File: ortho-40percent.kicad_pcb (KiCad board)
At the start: 2 copper layers, 229 x 81 mm, 128 parts, among them J1 USB-C_Receptacle-24, SW1 SW_NO_4-Pin, SW10 CherryMX, SW11 CherryMX, SW12 CherryMX, SW13 CherryMX, SW14 CherryMX, SW15 CherryMX, SW16 CherryMX, SW17 CherryMX, SW18 CherryMX, SW19 CherryMX, SW2 CherryMX, SW20 CherryMX, SW21 CherryMX, SW22 CherryMX, SW23 CherryMX, SW24 CherryMX, SW25 CherryMX, SW26 CherryMX, SW27 CherryMX, SW28 CherryMX, SW29 CherryMX, SW3 CherryMX, SW30 CherryMX, SW31 CherryMX, SW32 CherryMX, SW33 CherryMX, SW34 CherryMX, SW35 CherryMX, SW36 CherryMX, SW37 CherryMX, SW38 CherryMX, SW39 CherryMX, SW4 CherryMX, SW40 CherryMX, SW41 CherryMX, SW42 CherryMX, SW43 CherryMX, SW44 CherryMX, SW45 CherryMX, SW46 CherryMX, SW47 CherryMX, SW48 CherryMX, SW49 CherryMX, SW5 CherryMX, SW50 CherryMX, SW51 CherryMX, SW6 CherryMX, SW7 CherryMX, SW8 CherryMX, SW9 CherryMX, U1 U_TPD4E05U06DQAR, U2 U_ATmega32u4-MU, Y1 XTAL_4Lead

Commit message: Routing
more routing and placement
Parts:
- moved C4 57.4 mm to (210.0, 186.9)
- moved C5 56.2 mm to (213.0, 182.9)
- moved C1 54.5 mm to (215.0, 186.4), turned to 180 degrees
- moved C8 53.1 mm to (225.0, 187.4), turned to 90 degrees
- moved C7 49.7 mm to (237.0, 187.4), turned to 90 degrees
- moved Y1 47.8 mm to (219.0, 184.9)
- moved C2 47.5 mm to (215.0, 183.9), turned to 180 degrees
- moved C9 45.4 mm to (237.0, 181.9)
- moved C6 41.0 mm to (225.0, 182.4), turned to 270 degrees
- moved D34 10.7 mm to (204.5, 184.9)
- moved U2 8.51 mm to (231.0, 185.4), turned to 270 degrees
- moved R4 6.58 mm to (230.0, 178.9)
- moved R3 6.52 mm to (232.0, 178.9)
- moved D35 4.72 mm to (247.0, 190.9)
- moved L1 1.50 mm to (238.0, 167.4), turned to 90 degrees
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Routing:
- net VCC: track 0.00 -> 30.0 mm, vias 0 -> 6
- net DA+: track 0.00 -> 16.3 mm, vias 0 -> 2
- net DA-: track 0.00 -> 15.9 mm, vias 0 -> 2
- net VBUS: track 0.00 -> 7.28 mm, vias 0 -> 1
- net /D-: track 3.22 -> 6.30 mm
- net GND: track 1.42 -> 4.34 mm, vias 1 -> 0
- net /D+: track 6.30 -> 4.26 mm
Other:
- net class USB_diffPair added: clearance 0.2, trace_width 0.25, via_dia 0.8, via_drill 0.4

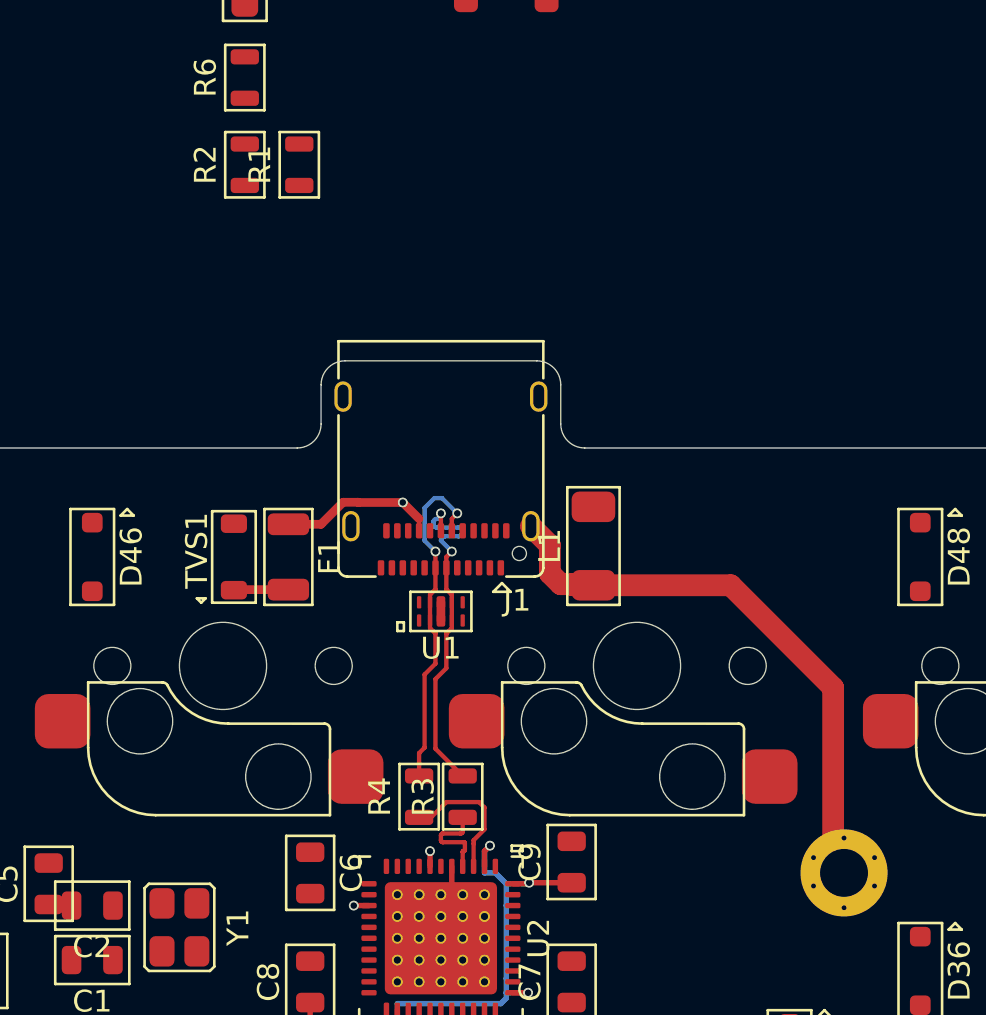
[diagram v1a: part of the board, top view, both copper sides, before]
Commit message: USB connections
Completed USB-C routing, tested ground planes and settings for robustness
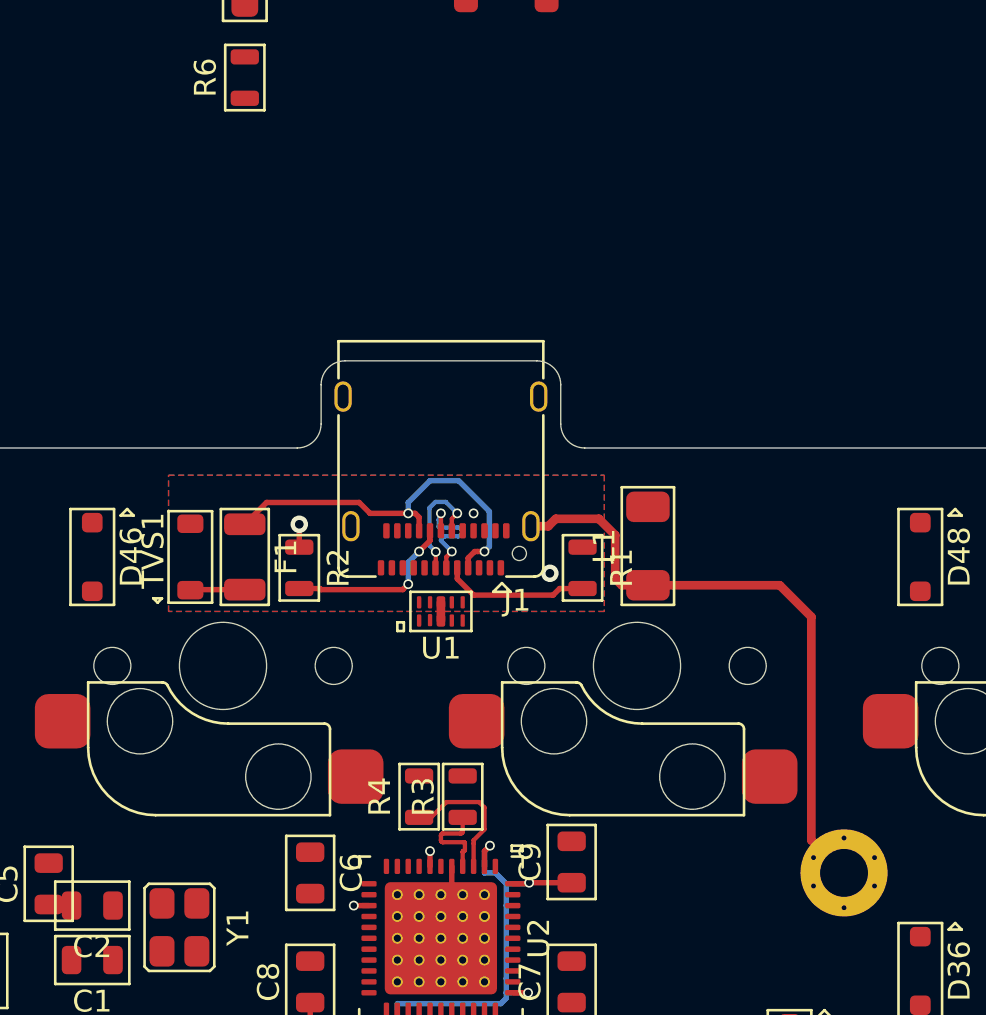
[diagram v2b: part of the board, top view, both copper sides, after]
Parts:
- moved R1 22.6 mm to (237.5, 168.4), turned to 270 degrees
- moved R2 18.7 mm to (224.5, 168.4), turned to 270 degrees
- moved L1 2.50 mm to (240.5, 167.4)
- moved F1 2.00 mm to (222.0, 167.9)
- moved TVS1 2.00 mm to (219.5, 167.9)
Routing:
- net DA+: track 16.3 -> 5.44 mm
- net DA-: track 15.9 -> 5.39 mm
- net VBUS: track 7.28 -> 17.8 mm, vias 1 -> 2
- net Net-(J1-PadB5): track 0.00 -> 7.99 mm, vias 0 -> 2
- net Net-(J1-PadA5): track 0.00 -> 6.68 mm
- net GNDPWR: track 26.4 -> 28.4 mm
- net GND: track 4.34 -> 5.39 mm, vias 0 -> 3
- added copper zone on B.Cu, net GND
- added copper zone on F.Cu, net GND

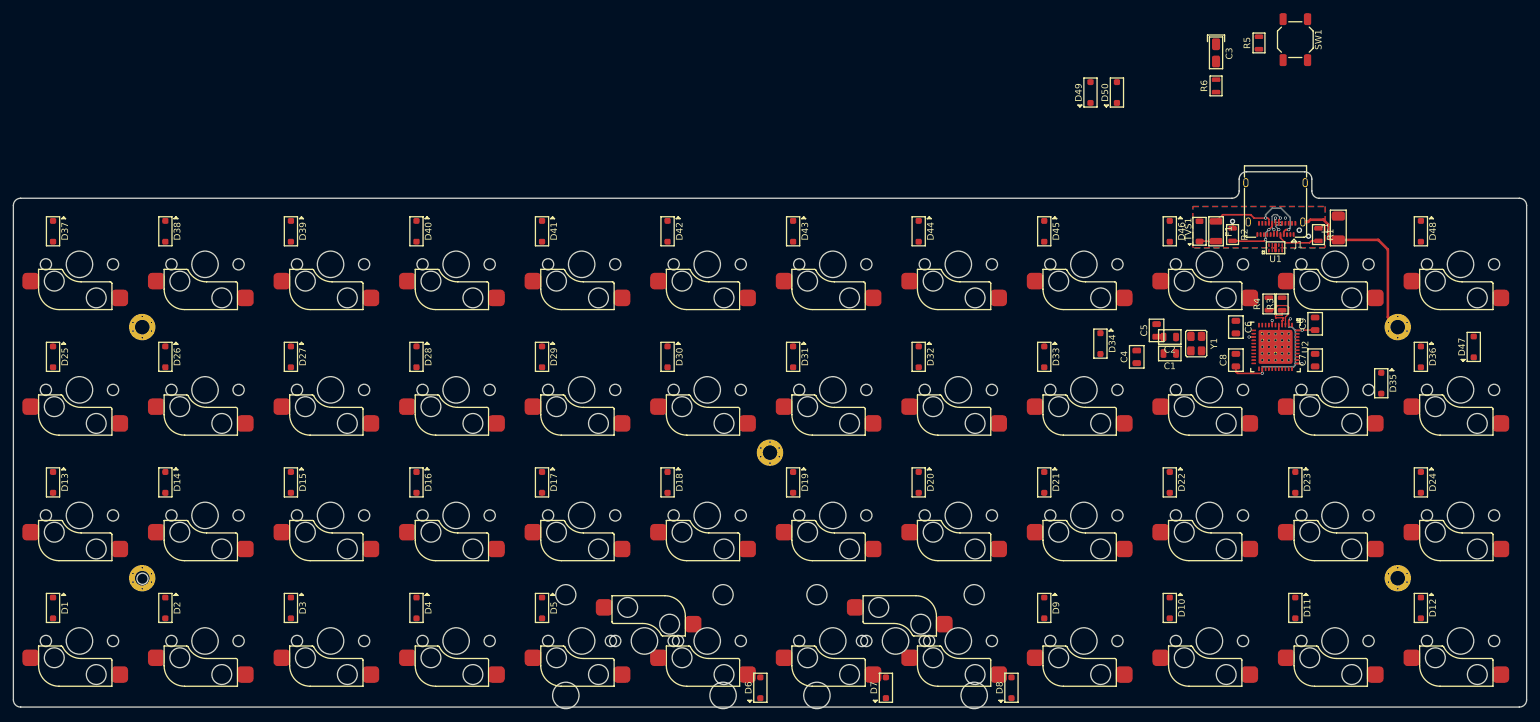
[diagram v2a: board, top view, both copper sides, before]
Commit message: Beginning switch routing
Finished routing of all micro, usb, and power components. Beginning placement and routing of diodes and keyswitches.
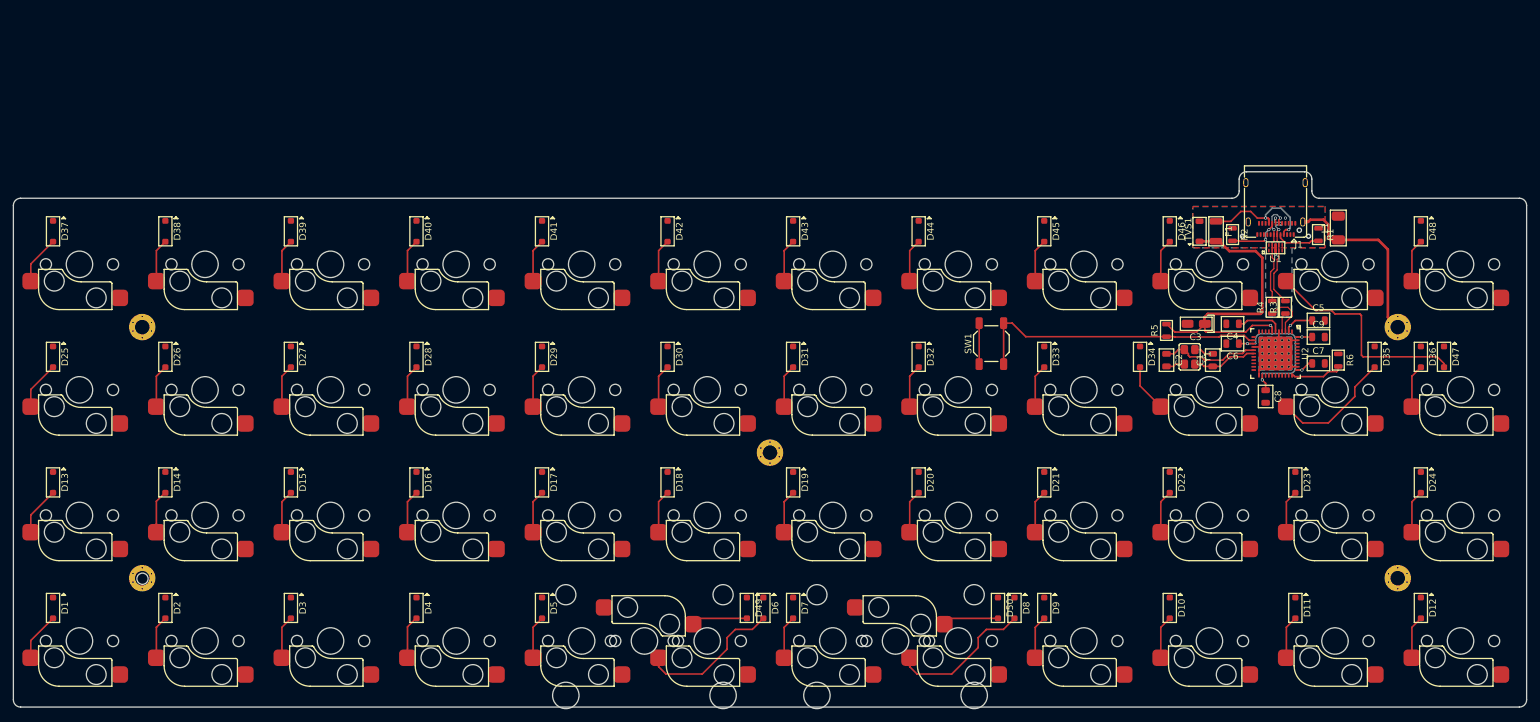
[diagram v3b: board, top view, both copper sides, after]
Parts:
- moved D49 93.7 mm to (151.0, 224.9), turned to 270 degrees
- moved D50 80.0 mm to (189.0, 224.9), turned to 270 degrees
- moved SW1 65.1 mm to (188.0, 184.9), turned to 0 degrees
- moved R5 45.7 mm to (214.5, 182.9)
- moved R6 45.4 mm to (240.5, 187.4), turned to 270 degrees
- moved C3 41.1 mm to (219.0, 181.9), turned to 180 degrees
- moved C5 24.5 mm to (237.5, 181.4), turned to 0 degrees
- moved D7 18.5 mm to (158.0, 224.9), turned to 270 degrees
- moved C4 15.3 mm to (224.5, 181.9), turned to 180 degrees
- moved D6 12.1 mm to (153.5, 224.9), turned to 270 degrees
- moved D8 12.1 mm to (191.5, 224.9), turned to 270 degrees
- moved C8 7.11 mm to (229.5, 192.9), turned to 270 degrees
- moved C1 6.58 mm to (221.5, 187.4), turned to 90 degrees
- moved D34 6.32 mm to (210.5, 186.9)
- moved D47 4.74 mm to (256.5, 186.9), turned to 270 degrees
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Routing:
- net VCC: track 30.0 -> 87.1 mm
- net Net-(R5-Pad1): track 0.00 -> 45.3 mm
- net Net-(D47-PadA): track 0.00 -> 33.1 mm
- net GND: track 5.39 -> 33.2 mm, vias 3 -> 4
- net Net-(D6-PadA): track 0.00 -> 22.2 mm
- net Net-(D8-PadA): track 0.00 -> 22.0 mm
- net Net-(D35-PadA): track 0.00 -> 18.7 mm
- net Net-(C2-Pad1): track 0.00 -> 14.9 mm
- net DA+: track 5.44 -> 16.6 mm
- net DA-: track 5.39 -> 16.0 mm
- net Net-(C1-Pad1): track 0.00 -> 9.85 mm
- net Net-(D50-PadA): track 0.00 -> 8.51 mm
- net Net-(D49-PadA): track 0.00 -> 8.51 mm
- net Net-(R6-Pad2): track 0.00 -> 8.05 mm
- net Net-(D37-PadA): track 0.00 -> 7.36 mm
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
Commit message: More key routing
Remapped keys to rows/columns to help optimize. Routed more.
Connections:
- D1 pad K: /KeyMatrix/ROW0 -> /KeyMatrix/ROW3
- D10 pad K: /KeyMatrix/ROW2 -> Net-(D10-PadK)
- D11 pad K: /KeyMatrix/ROW3 -> Net-(D11-PadK)
- D12 pad K: /KeyMatrix/ROW4 -> Net-(D12-PadK)
- D13 pad K: /KeyMatrix/ROW5 -> /KeyMatrix/ROW2
- D14 pad K: /KeyMatrix/ROW6 -> /KeyMatrix/ROW2
- D15 pad K: /KeyMatrix/ROW0 -> /KeyMatrix/ROW2
- D16 pad K: /KeyMatrix/ROW1 -> /KeyMatrix/ROW2
- D18 pad K: /KeyMatrix/ROW3 -> /KeyMatrix/ROW2
- D19 pad K: /KeyMatrix/ROW4 -> /KeyMatrix/ROW2
- D2 pad K: /KeyMatrix/ROW1 -> /KeyMatrix/ROW3
- D20 pad K: /KeyMatrix/ROW5 -> /KeyMatrix/ROW2
- D21 pad K: /KeyMatrix/ROW6 -> /KeyMatrix/ROW2
- D22 pad K: /KeyMatrix/ROW0 -> Net-(D22-PadK)
- D23 pad K: /KeyMatrix/ROW1 -> Net-(D23-PadK)
- D24 pad K: /KeyMatrix/ROW2 -> Net-(D24-PadK)
- D25 pad K: /KeyMatrix/ROW3 -> /KeyMatrix/ROW1
- D26 pad K: /KeyMatrix/ROW4 -> /KeyMatrix/ROW1
- D27 pad K: /KeyMatrix/ROW5 -> /KeyMatrix/ROW1
- D28 pad K: /KeyMatrix/ROW6 -> /KeyMatrix/ROW1
- D29 pad K: /KeyMatrix/ROW0 -> /KeyMatrix/ROW1
- D3 pad K: /KeyMatrix/ROW2 -> /KeyMatrix/ROW3
- D31 pad K: /KeyMatrix/ROW2 -> /KeyMatrix/ROW1
- D32 pad K: /KeyMatrix/ROW3 -> /KeyMatrix/ROW1
- D33 pad K: /KeyMatrix/ROW4 -> /KeyMatrix/ROW1
- D34 pad K: /KeyMatrix/ROW5 -> /KeyMatrix/ROW4
- D35 pad K: /KeyMatrix/ROW0 -> /KeyMatrix/ROW5
- D36 pad K: /KeyMatrix/ROW1 -> /KeyMatrix/ROW4
- D37 pad K: /KeyMatrix/ROW2 -> /KeyMatrix/ROW0
- D38 pad K: /KeyMatrix/ROW3 -> /KeyMatrix/ROW0
- D39 pad K: /KeyMatrix/ROW4 -> /KeyMatrix/ROW0
- D40 pad K: /KeyMatrix/ROW5 -> /KeyMatrix/ROW0
- D42 pad K: /KeyMatrix/ROW1 -> /KeyMatrix/ROW0
- D43 pad K: /KeyMatrix/ROW2 -> /KeyMatrix/ROW0
- D44 pad K: /KeyMatrix/ROW3 -> /KeyMatrix/ROW0
- D45 pad K: /KeyMatrix/ROW4 -> /KeyMatrix/ROW0
- D46 pad K: /KeyMatrix/ROW5 -> /KeyMatrix/ROW6
- D47 pad K: /KeyMatrix/ROW0 -> /KeyMatrix/ROW5
- D48 pad K: /KeyMatrix/ROW1 -> /KeyMatrix/ROW6
- D49 pad K: /KeyMatrix/ROW2 -> /KeyMatrix/ROW3
- D5 pad K: /KeyMatrix/ROW4 -> /KeyMatrix/ROW3
- D6 pad K: /KeyMatrix/ROW5 -> /KeyMatrix/ROW3
- D7 pad K: /KeyMatrix/ROW6 -> /KeyMatrix/ROW3
- D8 pad K: /KeyMatrix/ROW0 -> Net-(D8-PadK)
- D9 pad K: /KeyMatrix/ROW1 -> Net-(D9-PadK)
- SW10 pad 1: /KeyMatrix/COL1 -> Net-(SW10-Pad1)
- SW11 pad 1: /KeyMatrix/COL1 -> Net-(SW11-Pad1)
- SW12 pad 1: /KeyMatrix/COL1 -> Net-(SW12-Pad1)
- SW13 pad 1: /KeyMatrix/COL1 -> Net-(SW13-Pad1)
- SW14 pad 1: /KeyMatrix/COL1 -> /KeyMatrix/COL0
- SW17 pad 1: /KeyMatrix/COL2 -> /KeyMatrix/COL3
- SW18 pad 1: /KeyMatrix/COL2 -> /KeyMatrix/COL4
- SW19 pad 1: /KeyMatrix/COL2 -> /KeyMatrix/COL5
- SW20 pad 1: /KeyMatrix/COL2 -> /KeyMatrix/COL6
- SW21 pad 1: /KeyMatrix/COL2 -> /KeyMatrix/COL7
- SW22 pad 1: /KeyMatrix/COL2 -> /KeyMatrix/COL8
- SW23 pad 1: /KeyMatrix/COL3 -> Net-(SW23-Pad1)
- SW24 pad 1: /KeyMatrix/COL3 -> Net-(SW24-Pad1)
- SW25 pad 1: /KeyMatrix/COL3 -> Net-(SW25-Pad1)
- SW26 pad 1: /KeyMatrix/COL3 -> /KeyMatrix/COL0
- SW27 pad 1: /KeyMatrix/COL3 -> /KeyMatrix/COL1
- SW28 pad 1: /KeyMatrix/COL3 -> /KeyMatrix/COL2
- SW3 pad 1: /KeyMatrix/COL0 -> /KeyMatrix/COL1
- SW31 pad 1: /KeyMatrix/COL4 -> /KeyMatrix/COL5
- SW32 pad 1: /KeyMatrix/COL4 -> /KeyMatrix/COL6
- SW33 pad 1: /KeyMatrix/COL4 -> /KeyMatrix/COL7
- SW34 pad 1: /KeyMatrix/COL4 -> /KeyMatrix/COL8
- SW35 pad 1: /KeyMatrix/COL4 -> /KeyMatrix/COL2
- SW36 pad 1: /KeyMatrix/COL5 -> /KeyMatrix/COL2
- SW37 pad 1: /KeyMatrix/COL5 -> /KeyMatrix/COL0
- SW38 pad 1: /KeyMatrix/COL5 -> /KeyMatrix/COL0
- SW39 pad 1: /KeyMatrix/COL5 -> /KeyMatrix/COL1
- SW4 pad 1: /KeyMatrix/COL0 -> /KeyMatrix/COL2
- SW40 pad 1: /KeyMatrix/COL5 -> /KeyMatrix/COL2
- SW41 pad 1: /KeyMatrix/COL5 -> /KeyMatrix/COL3
- SW42 pad 1: /KeyMatrix/COL6 -> /KeyMatrix/COL4
- SW43 pad 1: /KeyMatrix/COL6 -> /KeyMatrix/COL5
- SW45 pad 1: /KeyMatrix/COL6 -> /KeyMatrix/COL7
- SW46 pad 1: /KeyMatrix/COL6 -> /KeyMatrix/COL8
- SW47 pad 1: /KeyMatrix/COL6 -> /KeyMatrix/COL1
- SW48 pad 1: /KeyMatrix/COL7 -> /KeyMatrix/COL0
- SW49 pad 1: /KeyMatrix/COL7 -> /KeyMatrix/COL0
- SW5 pad 1: /KeyMatrix/COL0 -> /KeyMatrix/COL3
- SW50 pad 1: /KeyMatrix/COL7 -> /KeyMatrix/COL4
- SW6 pad 1: /KeyMatrix/COL0 -> /KeyMatrix/COL5
- SW7 pad 1: /KeyMatrix/COL0 -> /KeyMatrix/COL6
- SW8 pad 1: /KeyMatrix/COL0 -> /KeyMatrix/COL8
- SW9 pad 1: /KeyMatrix/COL1 -> Net-(SW9-Pad1)
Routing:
- net /KeyMatrix/ROW1: track 0.00 -> 154.3 mm
- net /KeyMatrix/ROW2: track 0.00 -> 150.3 mm
- net /KeyMatrix/ROW0: track 0.00 -> 150.0 mm
- net /KeyMatrix/ROW3: track 0.00 -> 149.9 mm
- net /KeyMatrix/COL0: track 0.00 -> 67.7 mm, vias 0 -> 4
- net /KeyMatrix/COL2: track 0.00 -> 64.8 mm, vias 0 -> 4
- net /KeyMatrix/COL1: track 0.00 -> 64.8 mm, vias 0 -> 4
- net /KeyMatrix/COL3: track 0.00 -> 64.6 mm, vias 0 -> 4

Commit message: More routing
more routing
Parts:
- moved D6 1.00 mm to (154.5, 224.9)
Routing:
- net /KeyMatrix/COL5: track 0.00 -> 83.8 mm, vias 0 -> 5
- net /KeyMatrix/COL6: track 0.00 -> 82.6 mm, vias 0 -> 5
- net /KeyMatrix/COL7: track 0.00 -> 75.1 mm, vias 0 -> 5
- net /KeyMatrix/COL4: track 0.00 -> 57.0 mm, vias 0 -> 4
- net /KeyMatrix/COL8: track 0.00 -> 44.6 mm, vias 0 -> 3
- net Net-(D6-PadA): track 22.2 -> 23.9 mm
- net VCC: track 87.1 -> 86.1 mm

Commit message: More Routing
more routing
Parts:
- moved D8 1.00 mm to (192.5, 224.9)
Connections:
- D10 pad K: Net-(D10-PadK) -> /KeyMatrix/ROW3
- D11 pad K: Net-(D11-PadK) -> /KeyMatrix/ROW4
- D12 pad K: Net-(D12-PadK) -> /KeyMatrix/ROW4
- D22 pad K: Net-(D22-PadK) -> /KeyMatrix/ROW2
- D23 pad K: Net-(D23-PadK) -> /KeyMatrix/ROW5
- D24 pad K: Net-(D24-PadK) -> /KeyMatrix/ROW5
- D34 pad K: /KeyMatrix/ROW4 -> /KeyMatrix/ROW1
- D36 pad K: /KeyMatrix/ROW4 -> /KeyMatrix/ROW5
- D46 pad K: /KeyMatrix/ROW6 -> /KeyMatrix/ROW0
- D48 pad K: /KeyMatrix/ROW6 -> /KeyMatrix/ROW5
- D8 pad K: Net-(D8-PadK) -> /KeyMatrix/ROW4
- D9 pad K: Net-(D9-PadK) -> /KeyMatrix/ROW4
- SW10 pad 1: Net-(SW10-Pad1) -> /KeyMatrix/COL8
- SW11 pad 1: Net-(SW11-Pad1) -> /KeyMatrix/COL9
- SW12 pad 1: Net-(SW12-Pad1) -> /KeyMatrix/COL10
- SW13 pad 1: Net-(SW13-Pad1) -> /KeyMatrix/COL9
- SW23 pad 1: Net-(SW23-Pad1) -> /KeyMatrix/COL9
- SW24 pad 1: Net-(SW24-Pad1) -> /KeyMatrix/COL10
- SW25 pad 1: Net-(SW25-Pad1) -> /KeyMatrix/COL9
- SW35 pad 1: /KeyMatrix/COL2 -> /KeyMatrix/COL9
- SW36 pad 1: /KeyMatrix/COL2 -> /KeyMatrix/COL0
- SW37 pad 1: /KeyMatrix/COL0 -> /KeyMatrix/COL7
- SW47 pad 1: /KeyMatrix/COL1 -> /KeyMatrix/COL9
- SW48 pad 1: /KeyMatrix/COL0 -> /KeyMatrix/COL3
- SW49 pad 1: /KeyMatrix/COL0 -> /KeyMatrix/COL8
- SW51 pad 1: /KeyMatrix/COL7 -> /KeyMatrix/COL8
- SW8 pad 1: /KeyMatrix/COL8 -> /KeyMatrix/COL7
- SW9 pad 1: Net-(SW9-Pad1) -> /KeyMatrix/COL7
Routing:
- net /KeyMatrix/COL9: track 0.00 -> 119.2 mm, vias 0 -> 5
- net /KeyMatrix/ROW5: track 0.00 -> 76.4 mm, vias 0 -> 4
- net /KeyMatrix/COL8: track 44.6 -> 113.5 mm, vias 3 -> 4
- net /KeyMatrix/ROW4: track 0.00 -> 62.1 mm
- net /KeyMatrix/ROW3: track 149.9 -> 175.5 mm
- net /KeyMatrix/COL10: track 0.00 -> 19.4 mm, vias 0 -> 2
- net /KeyMatrix/ROW2: track 150.3 -> 169.3 mm
- net /KeyMatrix/ROW0: track 150.0 -> 169.0 mm
- net /KeyMatrix/ROW1: track 154.3 -> 168.8 mm
- net /KeyMatrix/COL7: track 75.1 -> 85.3 mm, vias 5 -> 4
- net Net-(D8-PadA): track 22.0 -> 22.6 mm
